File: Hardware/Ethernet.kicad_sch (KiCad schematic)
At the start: 39 parts, among them J1 Conn_01x07_Male, J10 SPI, J2 Conn_01x04_Male, J3 Conn_01x02_Male, J4 Conn_01x02_Male, J5 Conn_01x02_Male, J6 Conn_01x02_Male, J7 Conn_01x08_Male, J8 SPI, J9 QWIIC_Stackable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

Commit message: Working on SPI
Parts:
- removed J10: SPI, bare-footprints:8 pin jst 1.25 vertical, symbol Connector_Generic_MountingPin:Conn_01x08_MountingPin
- removed J8: SPI, Tinker:PinHeader_1x08_P1.27mm_Vertical, symbol Connector:Conn_01x08_Male
- J7: now in the parts list
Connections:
- net ATTACH is gone; now on net SCLK: J7.2 (Pin_2)
- net GPIO is gone; now on net ~{SCS}: J7.8 (Pin_8)
- net POWER_OK2 is gone; now on net MISO: J7.4 (Pin_4)
- net POWER_OK3 is gone; now on net MOSI: J7.6 (Pin_6)
- net RESET is gone; now on net WIZ_RST: J7.1 (Pin_1)
- net ALERT: no longer names the net of J7.7 (Pin_7)
- no-connect marks 5 -> 3
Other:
- note removed: "Control"
- note removed: "SPI JST"
- note removed: "SPI pin"
- moved on the sheet: J7, J9

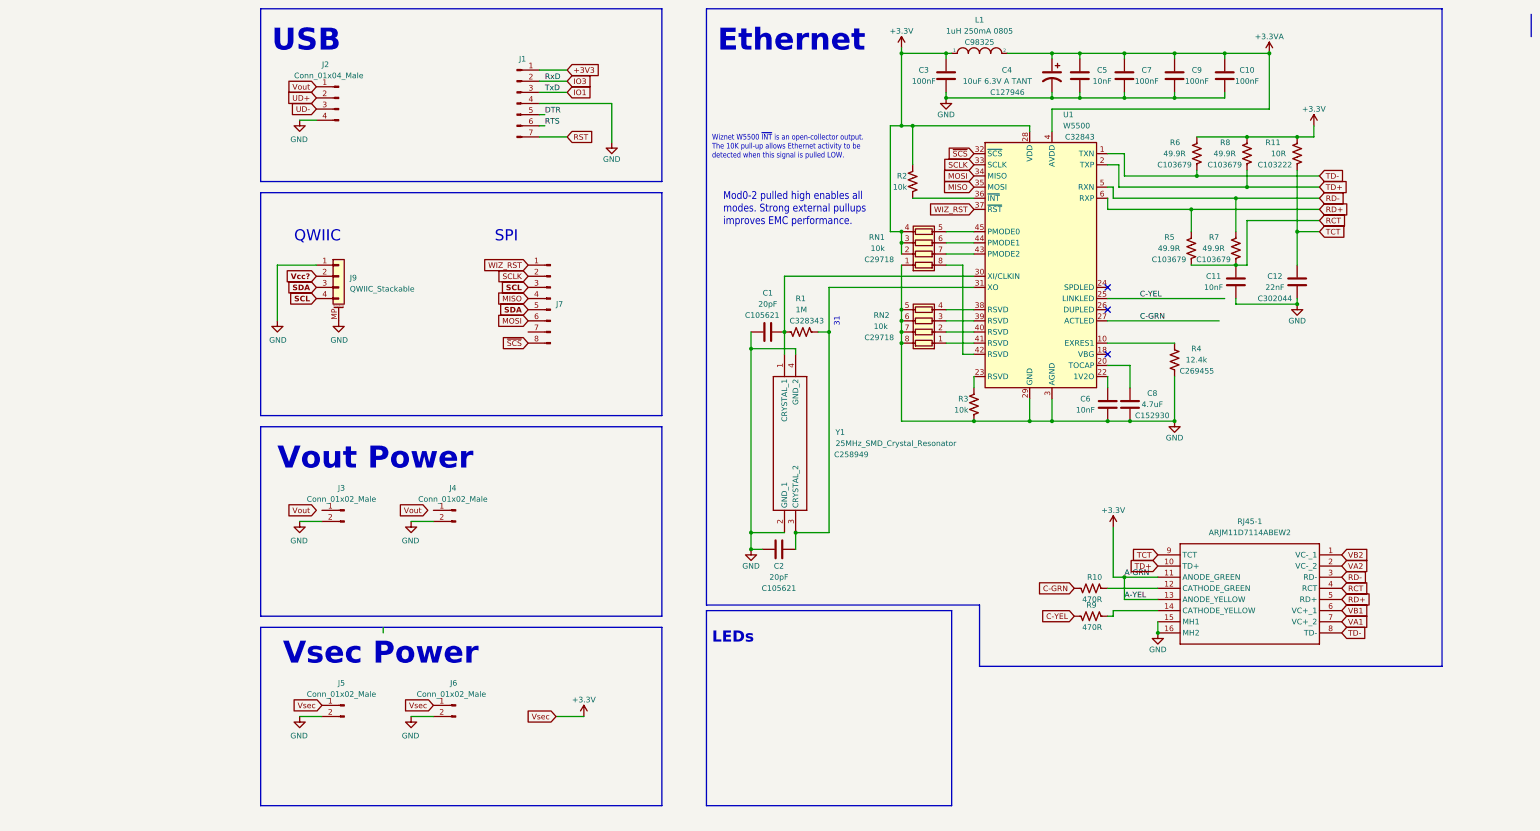
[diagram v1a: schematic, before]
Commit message: Refining the Ethernet board
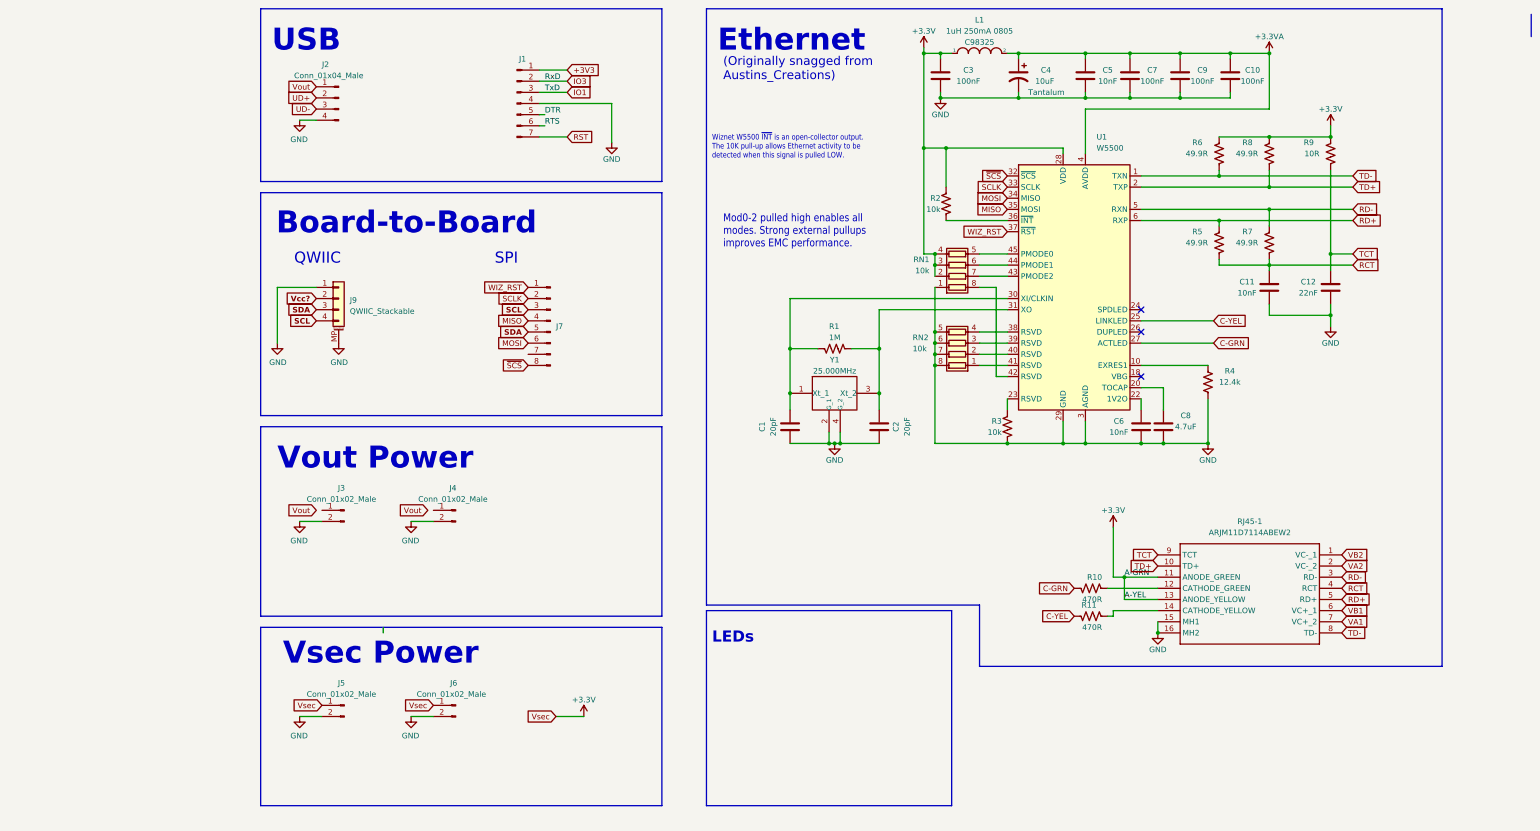
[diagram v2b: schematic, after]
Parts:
- removed Y1: 25MHz_SMD_Crystal_Resonator, Tinker:ABM825000MHz10B1UT, symbol Austins creations:25MHz_SMD_Crystal_Resonator
- added Y1: 25.000MHz, Tinker:ABM825000MHz10B1UT, symbol 0-TINKER Customs:ABM8-26.000MHz-20-D1X-T
- C4: value 10uF 6.3V A TANT -> 10uF; Type (none) -> Tantalum
- renumbered R9 to R11, R11 to R9
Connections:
- net GND: now also Y1.2 (G_1), Y1.4 (G_2)
- net at C1.2, R1.1, U1.30 (XI/CLKIN): now also Y1.1 (Xt_1)
- net at C2.2, R1.2, U1.31 (XO): now also Y1.3 (Xt_2)
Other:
- note added: "(Originally snagged from Austins_Creations)"
- note added: "Board-to-Board"
- note removed: "31"
- moved on the sheet: C1, C10, C11, C12, C2, C3, C4, C5, C6, C7, C8, C9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

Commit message: More on POE...
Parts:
- added J10, J11: Conn_01x02_Male, Connector_PinSocket_1.27mm:PinSocket_1x02_P1.27mm_Vertical_SMD_Pin1Right, symbol Connector:Conn_01x02_Male
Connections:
- net VA1: now also J11.1 (Pin_1)
- net VA2: now also J11.2 (Pin_2)
- net VB1: now also J10.1 (Pin_1)
- net VB2: now also J10.2 (Pin_2)
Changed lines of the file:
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@@
+    )
+  )
+  (global_label "VB2" (shape input) (at 157.48 128.27 180) (fields_autoplaced)
+    (effects (font (size 1.27 1.27)) (justify right))
+    (property "Intersheet References" "${INTERSHEET_REFS}" (id 0) (at 151.4988 128.1906 0)
+      (effects (font (size 1.27 1.27)) (justify right) hide)
     )
   )
@@
     )
   )
+  (global_label "VA1" (shape input) (at 156.21 139.7 180) (fields_autoplaced)
+    (effects (font (size 1.27 1.27)) (justify right))
+    (property "Intersheet References" "${INTERSHEET_REFS}" (id 0) (at 150.4102 139.6206 0)
+      (effects (font (size 1.27 1.27)) (justify right) hide)
+    )
+  )
   (global_label "RD+" (shape input) (at 260.35 148.59 0) (fields_autoplaced)
     (effects (font (size 1.27 1.27)) (justify left))
     (property "Intersheet References" "${INTERSHEET_REFS}" (id 0) (at 266.8755 148.5106 0)
       (effects (font (size 1.27 1.27)) (justify left) hide)
+    )
+  )
+  (global_label "VA2" (shape input) (at 156.21 142.24 180) (fields_autoplaced)
+    (effects (font (size 1.27 1.27)) (justify right))
+    (property "Intersheet References" "${INTERSHEET_REFS}" (id 0) (at 150.4102 142.1606 0)
+      (effects (font (size 1.27 1.27)) (justify right) hide)
     )
   )
@@
     (property "Intersheet References" "${INTERSHEET_REFS}" (id 0) (at 268.8107 72.3106 0)
       (effects (font (size 1.27 1.27)) (justify left) hide)
+    )
+  )
+  (global_label "VB1" (shape input) (at 157.48 125.73 180) (fields_autoplaced)
+    (effects (font (size 1.27 1.27)) (justify right))
+    (property "Intersheet References" "${INTERSHEET_REFS}" (id 0) (at 151.4988 125.6506 0)
+      (effects (font (size 1.27 1.27)) (justify right) hide)
     )
   )
@@
     (property "Type" "Tantalum" (id 5) (at 193.04 33.02 0))
     (property "LCSC" "C127946" (id 4) (at 199.39 33.02 0)
+      (effects (font (size 1.27 1.27)) hide)
+    )
+    (pin "1")
+    (pin "2")
+  )
+  (symbol (lib_id "Connector:Conn_01x02_Male") (at 161.29 139.7 0) (mirror y) (unit 1)
+    (in_bom no) (on_board yes)
+    (property "Reference" "J11" (id 0) (at 160.655 134.62 0))
+    (property "Value" "Conn_01x02_Male" (id 1) (at 160.655 137.16 0))
+    (property "Footprint" "Connector_PinSocket_1.27mm:PinSocket_1x02_P1.27mm_Vertical_SMD_Pin1Right" (id 2) (at 161.29 139.7 0)
+      (effects (font (size 1.27 1.27)) hide)
+    )
+    (property "Datasheet" "~" (id 3) (at 161.29 139.7 0)
       (effects (font (size 1.27 1.27)) hide)
     )
@@
     (pin "1")
   )
+  (symbol (lib_id "Connector:Conn_01x02_Male") (at 162.56 125.73 0) (mirror y) (unit 1)
+    (in_bom no) (on_board yes)
+    (property "Reference" "J10" (id 0) (at 161.925 120.65 0))
+    (property "Value" "Conn_01x02_Male" (id 1) (at 161.925 123.19 0))
+    (property "Footprint" "Connector_PinSocket_1.27mm:PinSocket_1x02_P1.27mm_Vertical_SMD_Pin1Right" (id 2) (at 162.56 125.73 0)
+      (effects (font (size 1.27 1.27)) hide)
+    )
+    (property "Datasheet" "~" (id 3) (at 162.56 125.73 0)
+      (effects (font (size 1.27 1.27)) hide)
+    )
+    (pin "1")
+    (pin "2")
+  )
   (symbol (lib_id "Connector:Conn_01x07_Male") (at 72.39 35.56 0) (unit 1)
     (in_bom no) (on_board no)
@@
       (reference "J9") (unit 1) (value "QWIIC_Stackable") (footprint "Tinker:QWIIC_Stack_II")
     )
+    (path "/a064da1d-e50b-4d46-9902-76208c1e200e"
+      (reference "J10") (unit 1) (value "Conn_01x02_Male") (footprint "Connector_PinSocket_1.27mm:PinSocket_1x02_P1.27mm_Vertical_SMD_Pin1Right")
+    )
+    (path "/504ed9d0-691d-452d-b516-7f09cf7e2eae"
+      (reference "J11") (unit 1) (value "Conn_01x02_Male") (footprint "Connector_PinSocket_1.27mm:PinSocket_1x02_P1.27mm_Vertical_SMD_Pin1Right")
+    )
     (path "/99ba0a0f-3edd-4786-889d-f6101a6723f5"

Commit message: Still migrating to 0.2.x
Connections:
- net MISO: now also J7.6 (Pin_6); no longer J7.4 (Pin_4)
- net MOSI: now also J7.8 (Pin_8); no longer J7.6 (Pin_6)
- net SCL: no longer J7.3 (Pin_3)
- net SCLK: now also J7.4 (Pin_4); no longer J7.2 (Pin_2)
- net SDA: no longer J7.5 (Pin_5)
- net ~{SCS}0: now reaches J7.7 (Pin_7)
- net ~{SCS}0: now also U1.32 (~{SCS})
- net WIZ_RST renamed ~{RESET}
- removed net ~{SCS}: J7.8 (Pin_8), U1.32 (~{SCS})
- new net RESET: J7.2 (Pin_2)
- new net ~{SCS}1: J7.5 (Pin_5)
- new net ~{SCS}2: J7.3 (Pin_3)
